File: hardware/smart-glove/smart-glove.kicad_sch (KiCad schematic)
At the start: 0 parts

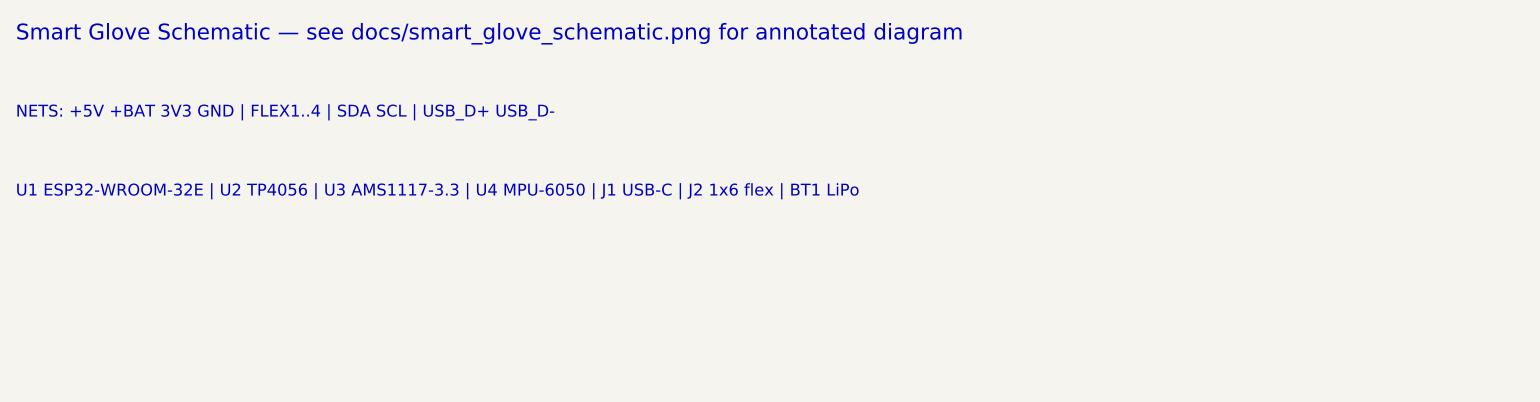
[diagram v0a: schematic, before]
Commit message: Make Smart Glove PCB fab-ready for prototype production
Generate a complete KiCad 7 board with library footprints (ESP32-WROOM-32,
TP4056, AMS1117, MPU-6050, USB-C, passives), nets, routing, and GND copper.

Export JLCPCB package: Gerbers, Excellon drill, BOM, CPL, fabrication notes,
production board preview, and automated design-check report.

Co-authored-by: ADIL ZAHOOR  <adilzahoor2812@users.noreply.github.com>
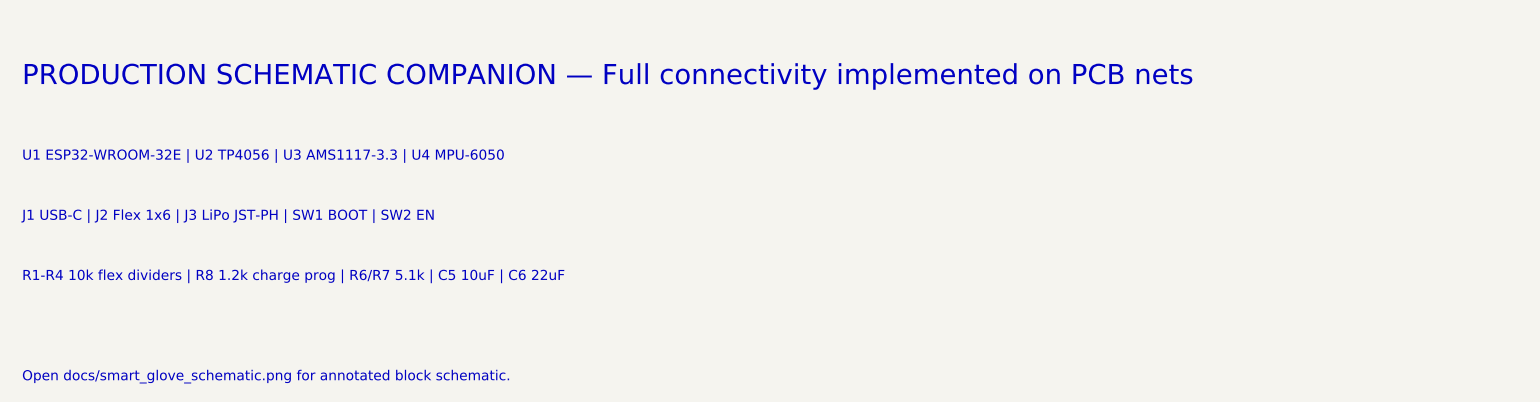
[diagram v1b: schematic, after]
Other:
- note added: "J1 USB-C | J2 Flex 1x6 | J3 LiPo JST-PH | SW1 BOOT | SW2 EN"
- note added: "Open docs/smart_glove_schematic.png for annotated block schematic."
- note added: "PRODUCTION SCHEMATIC COMPANION — Full connectivity implemented on PCB nets"
- note added: "R1-R4 10k flex dividers | R8 1.2k charge prog | R6/R7 5.1k | C5 10uF | C6 22uF"
- note added: "U1 ESP32-WROOM-32E | U2 TP4056 | U3 AMS1117-3.3 | U4 MPU-6050"
- note removed: "NETS: +5V +BAT 3V3 GND | FLEX1..4 | SDA SCL | USB_D+ USB_D-"
- note removed: "Smart Glove Schematic — see docs/smart_glove_schematic.png for annotated diagram"
- note removed: "U1 ESP32-WROOM-32E | U2 TP4056 | U3 AMS1117-3.3 | U4 MPU-6050 | J1 USB-C | J2 1x6 flex | BT1 LiPo"
- company: GetFly / Smart Glove -> GetFly
- title: Smart Glove Controller -> Smart Glove MCU Controller
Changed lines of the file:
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@@
-(kicad_sch
-  (version 20231120)
-  (generator "eeschema")
-  (generator_version "8.0")
+(kicad_sch (version 20230121) (generator eeschema)
   (paper "A3")
   (title_block
-    (title "Smart Glove Controller")
+    (title "Smart Glove MCU Controller")
     (date "2026-07-18")
     (rev "A")
-    (company "GetFly / Smart Glove")
-    (comment 1 "ESP32 + 4 flex channels + MPU6050 + TP4056")
-    (comment 2 "Reconstructed from project collage; photo labels illegible")
+    (company "GetFly")
+    (comment 1 "Production Rev A — ESP32 + 4 flex + MPU6050 + TP4056")
+    (comment 2 "See docs/PRODUCTION_NETLIST.md and fab/ for manufacturing package")
   )
-  (text "Smart Glove Schematic — see docs/smart_glove_schematic.png for annotated diagram"
-    (exclude_from_sim no) (exclude_from_bom no) (exclude_from_board no)
-    (at 50 20 0)
-    (effects (font (size 2 2)) (justify left))
+  (text "PRODUCTION SCHEMATIC COMPANION — Full connectivity implemented on PCB nets"
+    (at 50.8 25.4 0)
+    (effects (font (size 2.54 2.54)) (justify left))
   )
-  (text "NETS: +5V +BAT 3V3 GND | FLEX1..4 | SDA SCL | USB_D+ USB_D-"
-    (exclude_from_sim no) (exclude_from_bom no) (exclude_from_board no)
-    (at 50 30 0)
-    (effects (font (size 1.5 1.5)) (justify left))
+  (text "U1 ESP32-WROOM-32E | U2 TP4056 | U3 AMS1117-3.3 | U4 MPU-6050"
+    (at 50.8 35.56 0)
+    (effects (font (size 1.27 1.27)) (justify left))
   )
-  (text "U1 ESP32-WROOM-32E | U2 TP4056 | U3 AMS1117-3.3 | U4 MPU-6050 | J1 USB-C | J2 1x6 flex | BT1 LiPo"
-    (exclude_from_sim no) (exclude_from_bom no) (exclude_from_board no)
-    (at 50 40 0)
-    (effects (font (size 1.5 1.5)) (justify left))
+  (text "J1 USB-C | J2 Flex 1x6 | J3 LiPo JST-PH | SW1 BOOT | SW2 EN"
+    (at 50.8 43.18 0)
+    (effects (font (size 1.27 1.27)) (justify left))
+  )
+  (text "R1-R4 10k flex dividers | R8 1.2k charge prog | R6/R7 5.1k | C5 10uF | C6 22uF"
+    (at 50.8 50.8 0)
+    (effects (font (size 1.27 1.27)) (justify left))
+  )
+  (text "Open docs/smart_glove_schematic.png for annotated block schematic."
+    (at 50.8 63.5 0)
+    (effects (font (size 1.27 1.27)) (justify left))
   )
   (sheet_instances

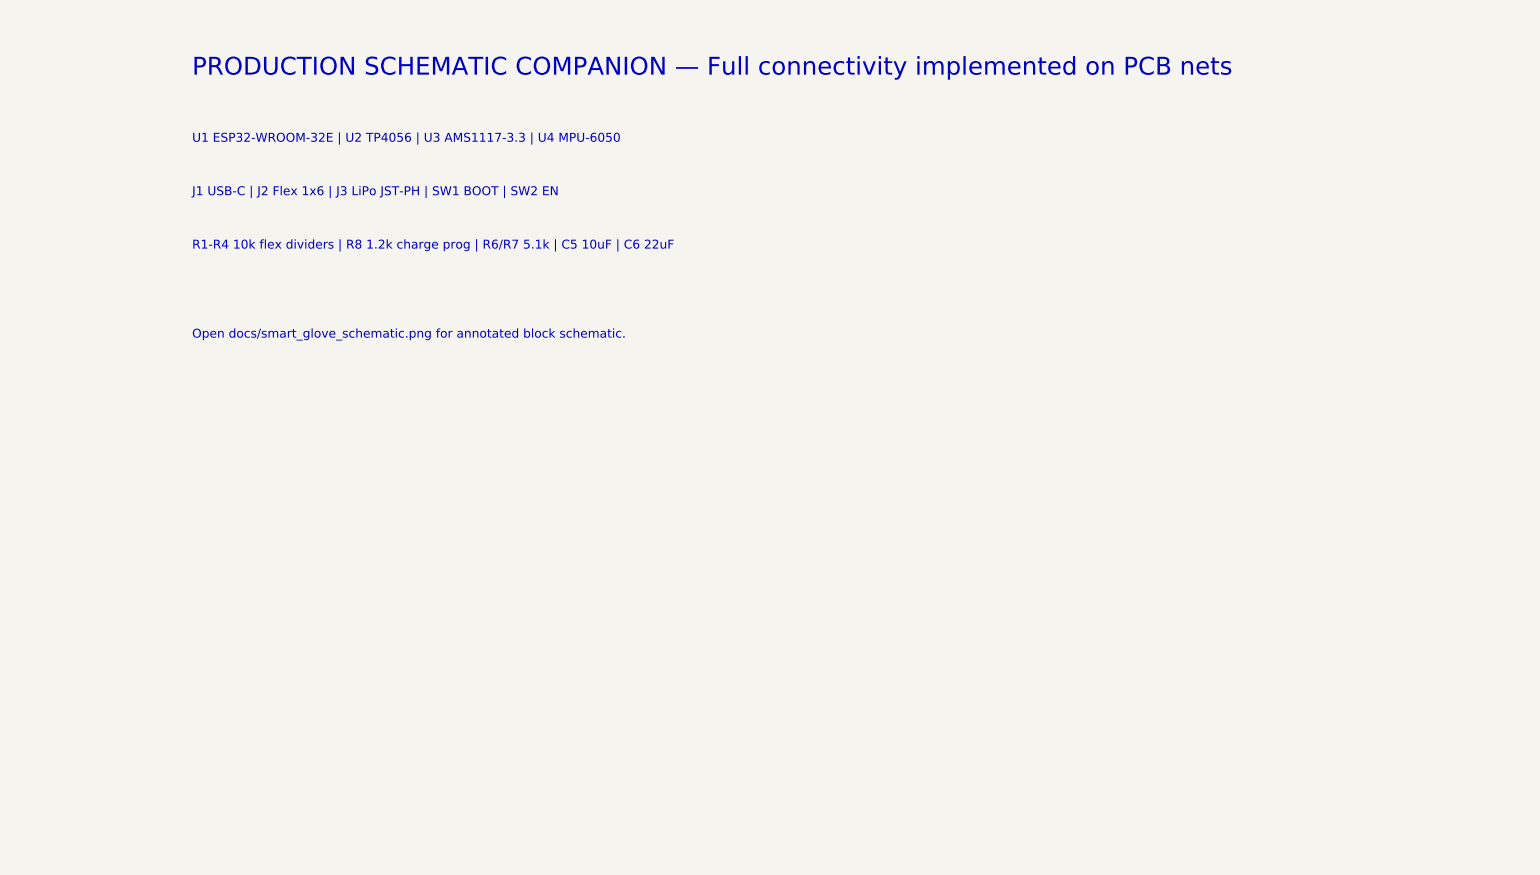
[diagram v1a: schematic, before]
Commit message: Compile ERC and DRC reports with KiCad 8 CLI
Run official sch erc and pcb drc on the Smart Glove project and save
text/json reports plus a compile summary under fab/.

Co-authored-by: ADIL ZAHOOR  <adilzahoor2812@users.noreply.github.com>
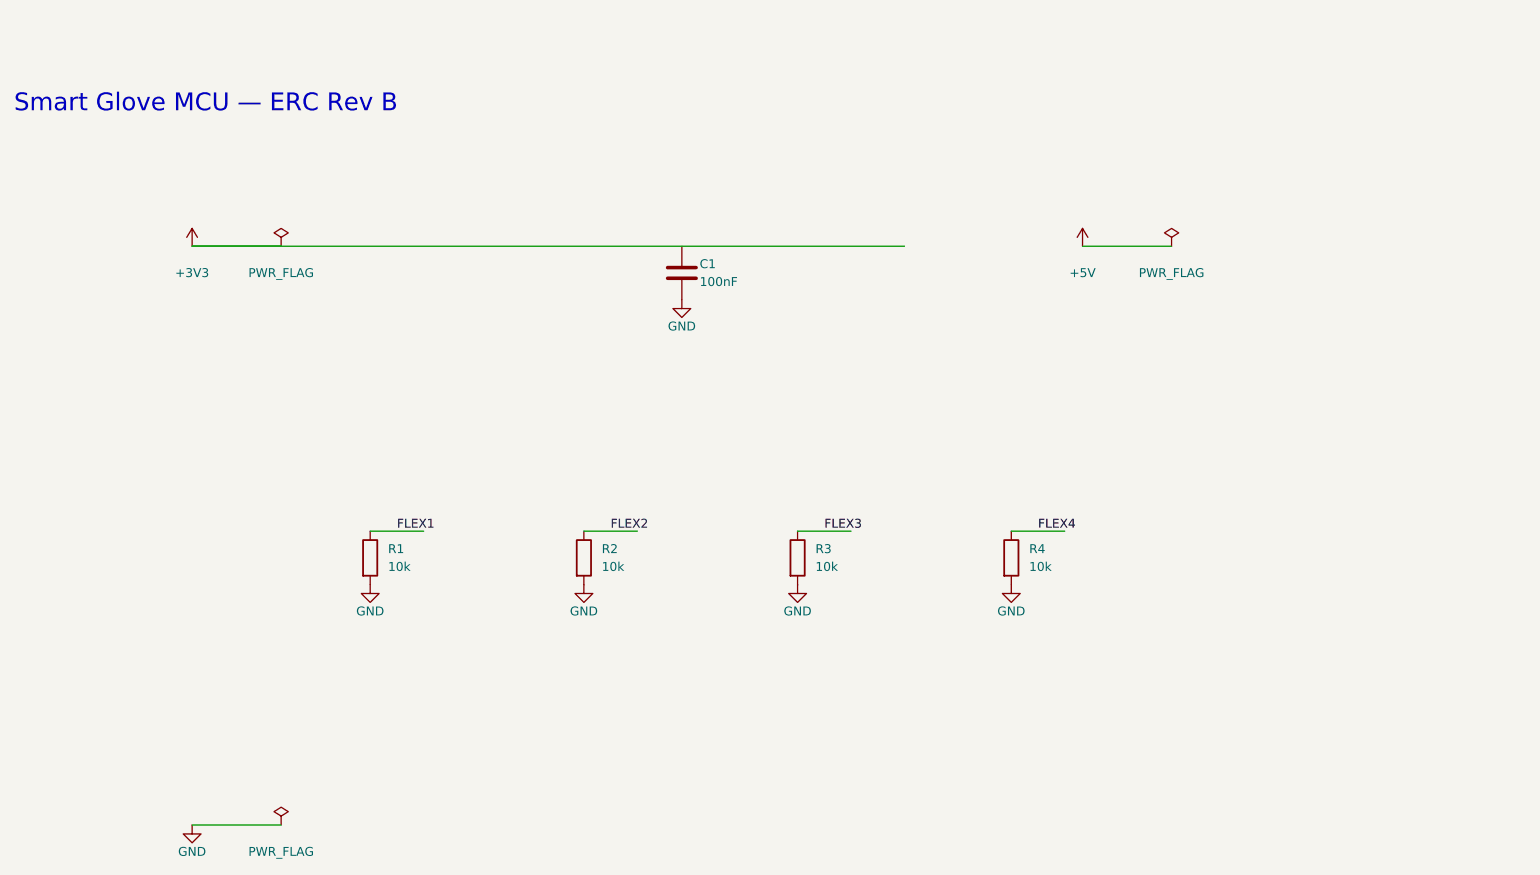
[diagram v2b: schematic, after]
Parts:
- added C1: 100nF, Capacitor_SMD:C_0603_1608Metric, symbol Device:C
- added R1, R2, R3, R4: 10k, Resistor_SMD:R_0603_1608Metric, symbol Device:R
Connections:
- new net FLEX1: R1.1
- new net FLEX2: R2.1
- new net FLEX3: R3.1
- new net FLEX4: R4.1
- new net GND: C1.2, R1.2, R2.2, R3.2, R4.2
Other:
- note added: "Smart Glove MCU — ERC Rev B"
- note removed: "J1 USB-C | J2 Flex 1x6 | J3 LiPo JST-PH | SW1 BOOT | SW2 EN"
- note removed: "Open docs/smart_glove_schematic.png for annotated block schematic."
- note removed: "PRODUCTION SCHEMATIC COMPANION — Full connectivity implemented on PCB nets"
- note removed: "R1-R4 10k flex dividers | R8 1.2k charge prog | R6/R7 5.1k | C5 10uF | C6 22uF"
- note removed: "U1 ESP32-WROOM-32E | U2 TP4056 | U3 AMS1117-3.3 | U4 MPU-6050"
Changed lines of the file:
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@@
-(kicad_sch (version 20230121) (generator eeschema)
+(kicad_sch
+  (version 20231120)
+  (generator "eeschema")
+  (generator_version "8.0")
   (paper "A3")
-  (title_block
-    (title "Smart Glove MCU Controller")
-    (date "2026-07-18")
-    (rev "A")
-    (company "GetFly")
-    (comment 1 "Production Rev A — ESP32 + 4 flex + MPU6050 + TP4056")
-    (comment 2 "See docs/PRODUCTION_NETLIST.md and fab/ for manufacturing package")
-  )
-  (text "PRODUCTION SCHEMATIC COMPANION — Full connectivity implemented on PCB nets"
-    (at 50.8 25.4 0)
-    (effects (font (size 2.54 2.54)) (justify left))
-  )
-  (text "U1 ESP32-WROOM-32E | U2 TP4056 | U3 AMS1117-3.3 | U4 MPU-6050"
-    (at 50.8 35.56 0)
-    (effects (font (size 1.27 1.27)) (justify left))
-  )
-  (text "J1 USB-C | J2 Flex 1x6 | J3 LiPo JST-PH | SW1 BOOT | SW2 EN"
-    (at 50.8 43.18 0)
-    (effects (font (size 1.27 1.27)) (justify left))
-  )
-  (text "R1-R4 10k flex dividers | R8 1.2k charge prog | R6/R7 5.1k | C5 10uF | C6 22uF"
-    (at 50.8 50.8 0)
-    (effects (font (size 1.27 1.27)) (justify left))
-  )
-  (text "Open docs/smart_glove_schematic.png for annotated block schematic."
-    (at 50.8 63.5 0)
-    (effects (font (size 1.27 1.27)) (justify left))
-  )
-  (sheet_instances
-    (path "/" (page "1"))
-  )
+  (title_block (title "Smart Glove MCU Controller") (date "2026-07-18") (rev "B") (company "GetFly"))
+  (symbol (lib_id "power:+3V3") (at 50.8 50.8 0) (unit 1)
+    (in_bom yes) (on_board yes) (dnp no)
+    (property "Reference" "#PWR01" (at 50.8 46.99 0) (effects (font (size 1.27 1.27)) hide))
+    (property "Value" "+3V3" (at 50.8 54.61 0) (effects (font (size 1.27 1.27))))
+    (pin "1"))
+  (symbol (lib_id "power:PWR_FLAG") (at 63.5 50.8 0) (unit 1)
+    (in_bom yes) (on_board yes) (dnp no)
+    (property "Reference" "#FLG01" (at 63.5 46.99 0) (effects (font (size 1.27 1.27)) hide))
+    (property "Value" "PWR_FLAG" (at 63.5 54.61 0) (effects (font (size 1.27 1.27))))
+    (pin "1"))
+  (wire (pts (xy 50.8 50.8) (xy 63.5 50.8)) (stroke (width 0) (type default)))
+  (wire (pts (xy 50.8 50.8) (xy 152.4 50.8)) (stroke (width 0) (type default)))
+  (symbol (lib_id "power:+5V") (at 177.8 50.8 0) (unit 1)
+    (in_bom yes) (on_board yes) (dnp no)
+    (property "Reference" "#PWR03" (at 177.8 46.99 0) (effects (font (size 1.27 1.27)) hide))
+    (property "Value" "+5V" (at 177.8 54.61 0) (effects (font (size 1.27 1.27))))
+    (pin "1"))
+  (symbol (lib_id "power:PWR_FLAG") (at 190.5 50.8 0) (unit 1)
+    (in_bom yes) (on_board yes) (dnp no)
+    (property "Reference" "#FLG03" (at 190.5 46.99 0) (effects (font (size 1.27 1.27)) hide))
+    (property "Value" "PWR_FLAG" (at 190.5 54.61 0) (effects (font (size 1.27 1.27))))
+    (pin "1"))
+  (wire (pts (xy 177.8 50.8) (xy 190.5 50.8)) (stroke (width 0) (type default)))
+  (symbol (lib_id "power:GND") (at 50.8 133.35 0) (unit 1)
+    (in_bom yes) (on_board yes) (dnp no)
+    (property "Reference" "#PWR02" (at 50.8 139.7 0) (effects (font (size 1.27 1.27)) hide))
+    (property "Value" "GND" (at 50.8 137.16 0) (effects (font (size 1.27 1.27))))
+    (pin "1"))
+  (symbol (lib_id "power:PWR_FLAG") (at 63.5 133.35 0) (unit 1)
+    (in_bom yes) (on_board yes) (dnp no)
+    (property "Reference" "#FLG02" (at 63.5 139.7 0) (effects (font (size 1.27 1.27)) hide))
+    (property "Value" "PWR_FLAG" (at 63.5 137.16 0) (effects (font (size 1.27 1.27))))
+    (pin "1"))
+  (wire (pts (xy 50.8 133.35) (xy 63.5 133.35)) (stroke (width 0) (type default)))
+  (symbol (lib_id "Device:R") (at 76.2 95.25 0) (unit 1)
+      (in_bom yes) (on_board yes) (dnp no)
+      (property "Reference" "R1" (at 78.74000000000001 93.98 0) (effects (font (size 1.27 1.27)) (justify left)))
+      (property "Value" "10k" (at 78.74000000000001 96.52 0) (effects (font (size 1.27 1.27)) (justify left)))
+      (property "Footprint" "Resistor_SMD:R_0603_1608Metric" (at 76.2 95.25 90) (effects (font (size 1.27 1.27)) hide))
+      (property "Datasheet" "~" (at 76.2 95.25 0) (effects (font (size 1.27 1.27)) hide))
+      (pin "1") (pin "2"))
+  (wire (pts (xy 76.2 91.44) (xy 83.82000000000001 91.44)) (stroke (width 0) (type default)))
+  (label "FLEX1" (at 80.01 91.44 0) (effects (font (size 1.27 1.27)) (justify left bottom)))
+  (symbol (lib_id "power:GND") (at 76.2 99.06 0) (unit 1)
+      (in_bom yes) (on_board yes) (dnp no)
+      (property "Reference" "#R1G" (at 76.2 104.14 0) (effects (font (size 1.27 1.27)) hide))
+      (property "Value" "GND" (at 76.2 102.87 0) (effects (font (size 1.27 1.27))))
+      (pin "1"))
+  (symbol (lib_id "Device:R") (at 106.68 95.25 0) (unit 1)
+      (in_bom yes) (on_board yes) (dnp no)
+      (property "Reference" "R2" (at 109.22000000000001 93.98 0) (effects (font (size 1.27 1.27)) (justify left)))
+      (property "Value" "10k" (at 109.22000000000001 96.52 0) (effects (font (size 1.27 1.27)) (justify left)))
+      (property "Footprint" "Resistor_SMD:R_0603_1608Metric" (at 106.68 95.25 90) (effects (font (size 1.27 1.27)) hide))
+      (property "Datasheet" "~" (at 106.68 95.25 0) (effects (font (size 1.27 1.27)) hide))
+      (pin "1") (pin "2"))
+  (wire (pts (xy 106.68 91.44) (xy 114.30000000000001 91.44)) (stroke (width 0) (type default)))
+  (label "FLEX2" (at 110.49000000000001 91.44 0) (effects (font (size 1.27 1.27)) (justify left bottom)))
+  (symbol (lib_id "power:GND") (at 106.68 99.06 0) (unit 1)
+      (in_bom yes) (on_board yes) (dnp no)
+      (property "Reference" "#R2G" (at 106.68 104.14 0) (effects (font (size 1.27 1.27)) hide))
+      (property "Value" "GND" (at 106.68 102.87 0) (effects (font (size 1.27 1.27))))
+      (pin "1"))
+  (symbol (lib_id "Device:R") (at 137.16 95.25 0) (unit 1)
+      (in_bom yes) (on_board yes) (dnp no)
+      (property "Reference" "R3" (at 139.7 93.98 0) (effects (font (size 1.27 1.27)) (justify left)))
+      (property "Value" "10k" (at 139.7 96.52 0) (effects (font (size 1.27 1.27)) (justify left)))
+      (property "Footprint" "Resistor_SMD:R_0603_1608Metric" (at 137.16 95.25 90) (effects (font (size 1.27 1.27)) hide))
+      (property "Datasheet" "~" (at 137.16 95.25 0) (effects (font (size 1.27 1.27)) hide))
+      (pin "1") (pin "2"))
+  (wire (pts (xy 137.16 91.44) (xy 144.78 91.44)) (stroke (width 0) (type default)))
+  (label "FLEX3" (at 140.97 91.44 0) (effects (font (size 1.27 1.27)) (justify left bottom)))
+  (symbol (lib_id "power:GND") (at 137.16 99.06 0) (unit 1)
+      (in_bom yes) (on_board yes) (dnp no)
+      (property "Reference" "#R3G" (at 137.16 104.14 0) (effects (font (size 1.27 1.27)) hide))
+      (property "Value" "GND" (at 137.16 102.87 0) (effects (font (size 1.27 1.27))))
+      (pin "1"))
+  (symbol (lib_id "Device:R") (at 167.64 95.25 0) (unit 1)
+      (in_bom yes) (on_board yes) (dnp no)
+      (property "Reference" "R4" (at 170.17999999999998 93.98 0) (effects (font (size 1.27 1.27)) (justify left)))
+      (property "Value" "10k" (at 170.17999999999998 96.52 0) (effects (font (size 1.27 1.27)) (justify left)))
+      (property "Footprint" "Resistor_SMD:R_0603_1608Metric" (at 167.64 95.25 90) (effects (font (size 1.27 1.27)) hide))
+      (property "Datasheet" "~" (at 167.64 95.25 0) (effects (font (size 1.27 1.27)) hide))
+      (pin "1") (pin "2"))
+  (wire (pts (xy 167.64 91.44) (xy 175.26 91.44)) (stroke (width 0) (type default)))
+  (label "FLEX4" (at 171.45 91.44 0) (effects (font (size 1.27 1.27)) (justify left bottom)))
+  (symbol (lib_id "power:GND") (at 167.64 99.06 0) (unit 1)
+      (in_bom yes) (on_board yes) (dnp no)
+      (property "Reference" "#R4G" (at 167.64 104.14 0) (effects (font (size 1.27 1.27)) hide))
+      (property "Value" "GND" (at 167.64 102.87 0) (effects (font (size 1.27 1.27))))
+      (pin "1"))
+  (symbol (lib_id "Device:C") (at 120.65 54.61 0) (unit 1)
+    (in_bom yes) (on_board yes) (dnp no)
+    (property "Reference" "C1" (at 123.19000000000001 53.339999999999996 0) (effects (font (size 1.27 1.27)) (justify left)))
+    (property "Value" "100nF" (at 123.19000000000001 55.88 0) (effects (font (size 1.27 1.27)) (justify left)))
+    (property "Footprint" "Capacitor_SMD:C_0603_1608Metric" (at 120.65 54.61 0) (effects (font (size 1.27 1.27)) hide))
+    (property "Datasheet" "~" (at 120.65 54.61 0) (effects (font (size 1.27 1.27)) hide))
+    (pin "1") (pin "2"))
+  (symbol (lib_id "power:GND") (at 120.65 58.42 0) (unit 1)
+    (in_bom yes) (on_board yes) (dnp no)
+    (property "Reference" "#C1G" (at 120.65 63.5 0) (effects (font (size 1.27 1.27)) hide))
+    (property "Value" "GND" (at 120.65 62.230000000000004 0) (effects (font (size 1.27 1.27))))
+    (pin "1"))
+  (text "Smart Glove MCU — ERC Rev B" (at 25.4 30.48 0) (effects (font (size 2.54 2.54)) (justify left)))
+  (sheet_instances (path "/" (page "1")))
 )
